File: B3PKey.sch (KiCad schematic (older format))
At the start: 180 parts, among them SW1 SW_Push, U1 ATmega32U4-AU, Y1 16MHz

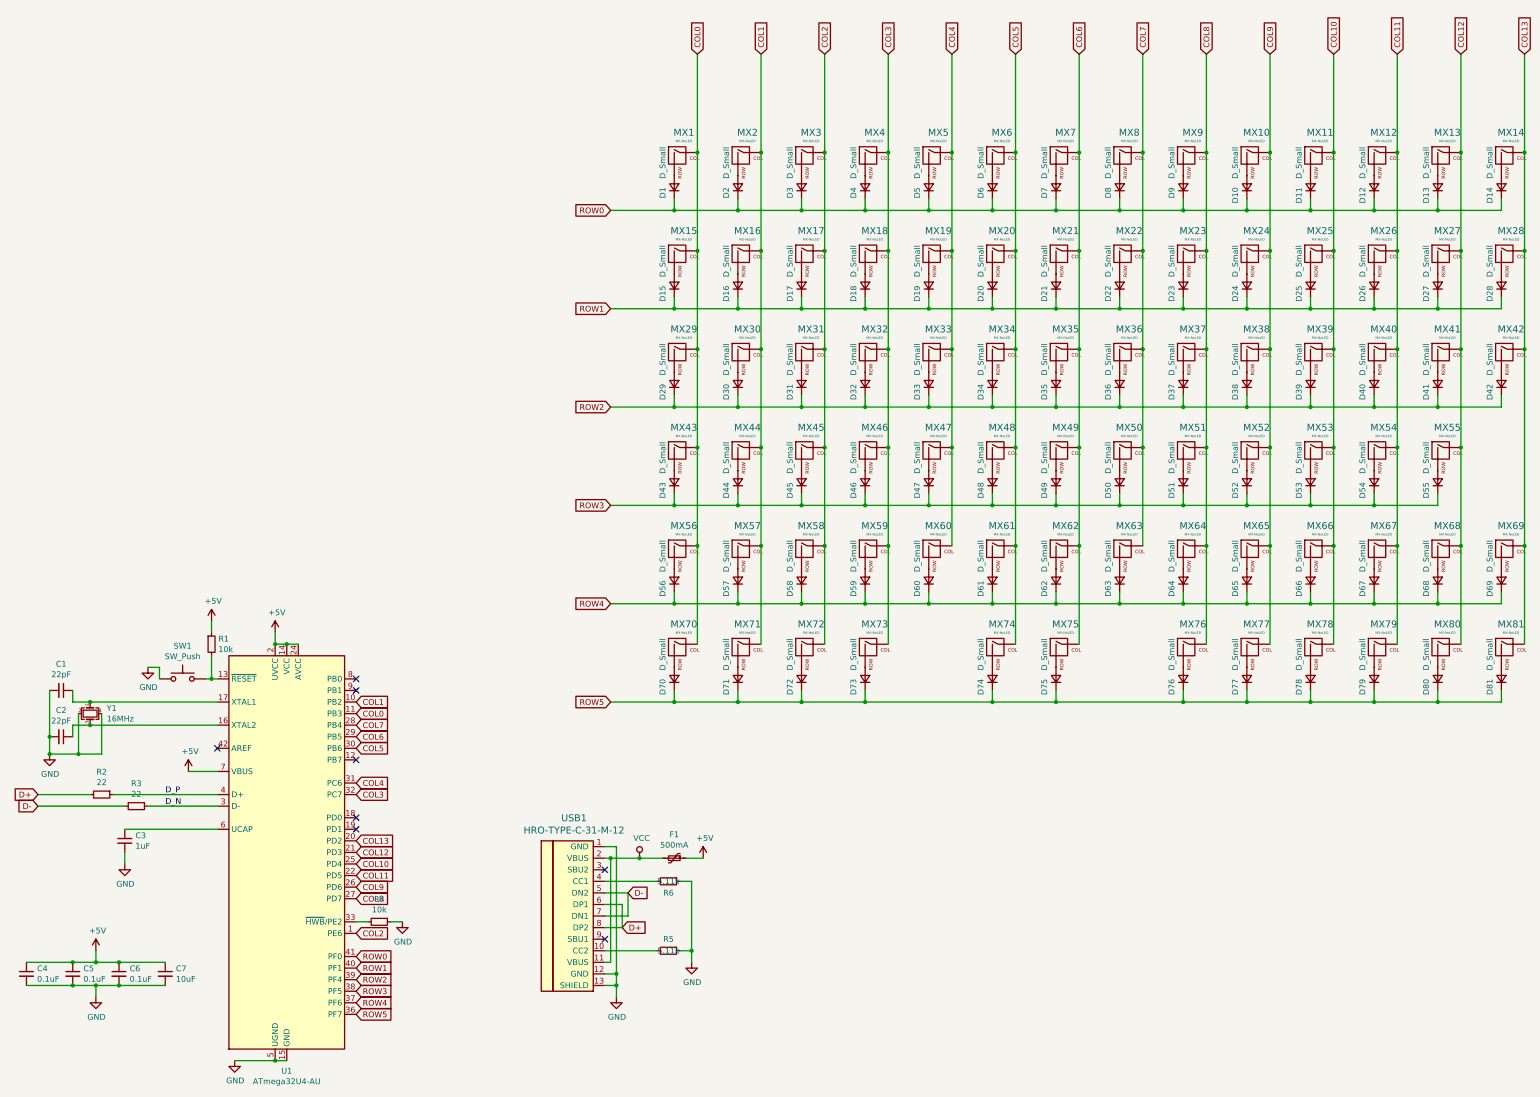
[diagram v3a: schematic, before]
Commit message: Move components to spacebar
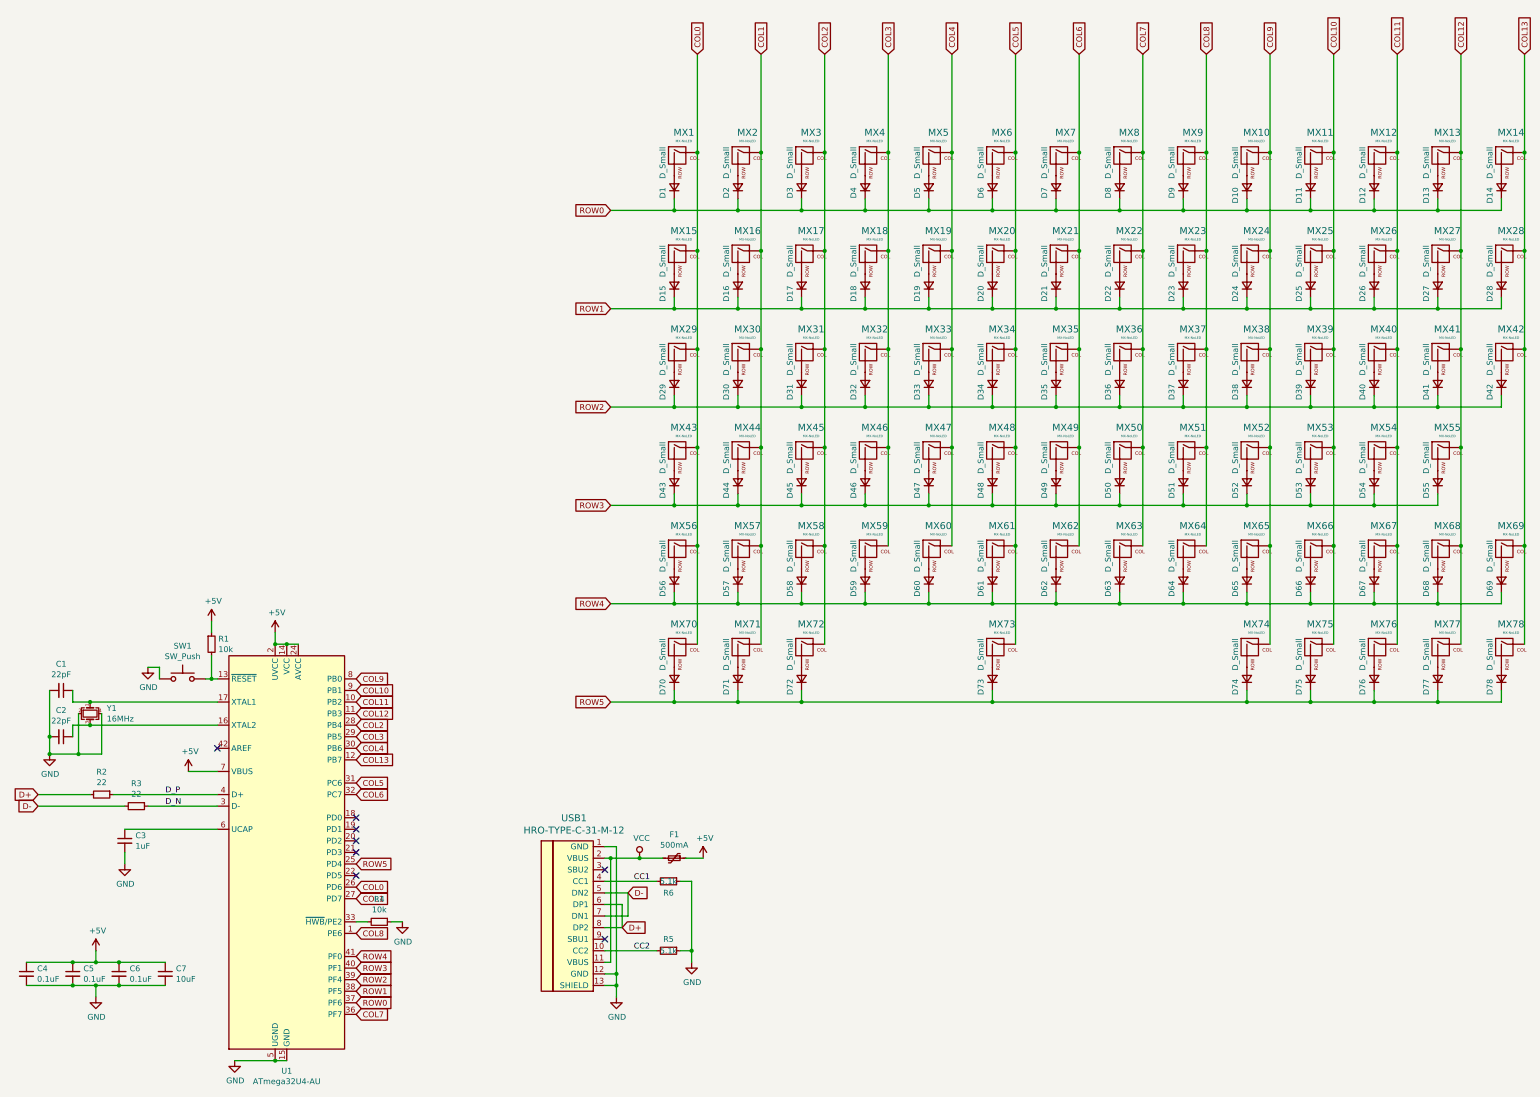
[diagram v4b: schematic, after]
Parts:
- removed D79, D80, D81: D_Small, Diode_SMD:D_SOD-123, symbol Device:D_Small
- removed MX79, MX80, MX81: MX-NoLED, MX_Only:MXOnly-1U-NoLED, symbol MX_Alps_Hybrid:MX-NoLED
- D1, D10, D11, D12, D13, D14, D15, D16, D17, D18, D19, D2, D20, D21, D22, D23, D24, D25, D26, D27, D28, D29, D3, D30, D31, D32, D33, D34, D35, D36, D37, D38, D39, D4, D40, D41, D42, D43, D44, D45, D46, D47, D48, D49, D5, D50, D51, D52, D53, D54, D55, D56, D57, D58, D59, D6, D60, D61, D62, D63, D64, D65, D66, D67, D68, D69, D7, D70, D71, D72, D73, D74, D75, D76, D77, D78, D8, D9: footprint Diode_SMD:D_SOD-123 -> Diode_THT:D_DO-35_SOD27_P7.62mm_Horizontal
- MX73: footprint MX_Only:MXOnly-1U-NoLED -> MX_Only:MXOnly-6U-Centered-ReversedStabilizers-NoLED
- MX74, MX75: footprint MX_Only:MXOnly-2U-ReversedStabilizers-NoLED -> MX_Only:MXOnly-1U-NoLED
- R5, R6: value 5.11k -> 5.1k
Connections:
- net COL0: now also U1.26 (PD6); no longer U1.11 (PB3)
- net COL1: now also U1.27 (PD7); no longer U1.10 (PB2)
- net COL10: now also MX75.1 (COL), U1.9 (PB1); no longer MX78.1 (COL), U1.25 (PD4)
- net COL11: now also MX76.1 (COL), U1.10 (PB2); no longer U1.22 (PD5)
- net COL12: now also MX77.1 (COL), U1.11 (PB3); no longer U1.21 (PD3)
- net COL13: now also MX78.1 (COL), U1.12 (PB7); no longer U1.20 (PD2)
- net COL2: now also U1.28 (PB4); no longer U1.1 (PE6)
- net COL3: now also U1.29 (PB5); no longer MX73.1 (COL), U1.32 (PC7)
- net COL4: now also U1.30 (PB6); no longer U1.31 (PC6)
- net COL5: now also MX73.1 (COL), U1.31 (PC6); no longer MX74.1 (COL), U1.30 (PB6)
- net COL6: now also U1.32 (PC7); no longer MX75.1 (COL), U1.29 (PB5)
- net COL7: now also U1.36 (PF7); no longer U1.28 (PB4)
- net COL8: now also U1.1 (PE6); no longer MX76.1 (COL), U1.27 (PD7)
- net COL9: now also MX74.1 (COL), U1.8 (PB0); no longer MX77.1 (COL), U1.26 (PD6)
- net ROW0: now also U1.37 (PF6); no longer U1.41 (PF0)
- net ROW1: now also U1.38 (PF5); no longer U1.40 (PF1)
- net ROW3: now also U1.40 (PF1); no longer U1.38 (PF5)
- net ROW4: now also U1.41 (PF0); no longer U1.37 (PF6)
- net ROW5: now also U1.25 (PD4); no longer U1.36 (PF7)
- net CC2: now reaches R5.2, USB1.10 (CC2)
- net CC1: now reaches R6.2, USB1.4 (CC1)
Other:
- moved on the sheet: D73, D74, D75, D76, D77, D78, MX73, MX74, MX75, MX76, MX77, MX78

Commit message: Update pbc outline, small tweaks
Also generate new gerbers and add case_open dxf file
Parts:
- D1, D10, D11, D12, D13, D14, D15, D16, D17, D18, D19, D2, D20, D21, D22, D23, D24, D25, D26, D27, D28, D29, D3, D30, D31, D32, D33, D34, D35, D36, D37, D38, D39, D4, D40, D41, D42, D43, D44, D45, D46, D47, D48, D49, D5, D50, D51, D52, D53, D54, D55, D56, D57, D58, D59, D6, D60, D61, D62, D63, D64, D65, D66, D67, D68, D69, D7, D70, D71, D72, D73, D74, D75, D76, D77, D78, D8, D9: footprint Diode_THT:D_DO-35_SOD27_P7.62mm_Horizontal -> Diode_SMD:D_SOD-123
- MX73: footprint MX_Only:MXOnly-6U-Centered-ReversedStabilizers-NoLED -> MX_Only:MXOnly-6U-ReversedStabilizers-NoLED
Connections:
- net COL5: no longer MX73.1 (COL)
- net COL6: now also MX73.1 (COL)
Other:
- moved on the sheet: D73, MX73
